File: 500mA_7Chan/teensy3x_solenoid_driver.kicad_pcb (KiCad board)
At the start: 2 copper layers, 88.9 x 50.8 mm, 16 parts, among them J1 Conn_01x02, J2 Conn_01x02, J3 Conn_01x02, J4 Conn_01x02, J5 Conn_01x02, J6 Conn_01x02, J7 Conn_01x02, J8 Conn_02x05_Odd_Even, J9 Jack-DC, M1 VAL**, M2 VAL**, M3 VAL**, M4 VAL**, U1 TEENSY3x, U2 TBD62003A

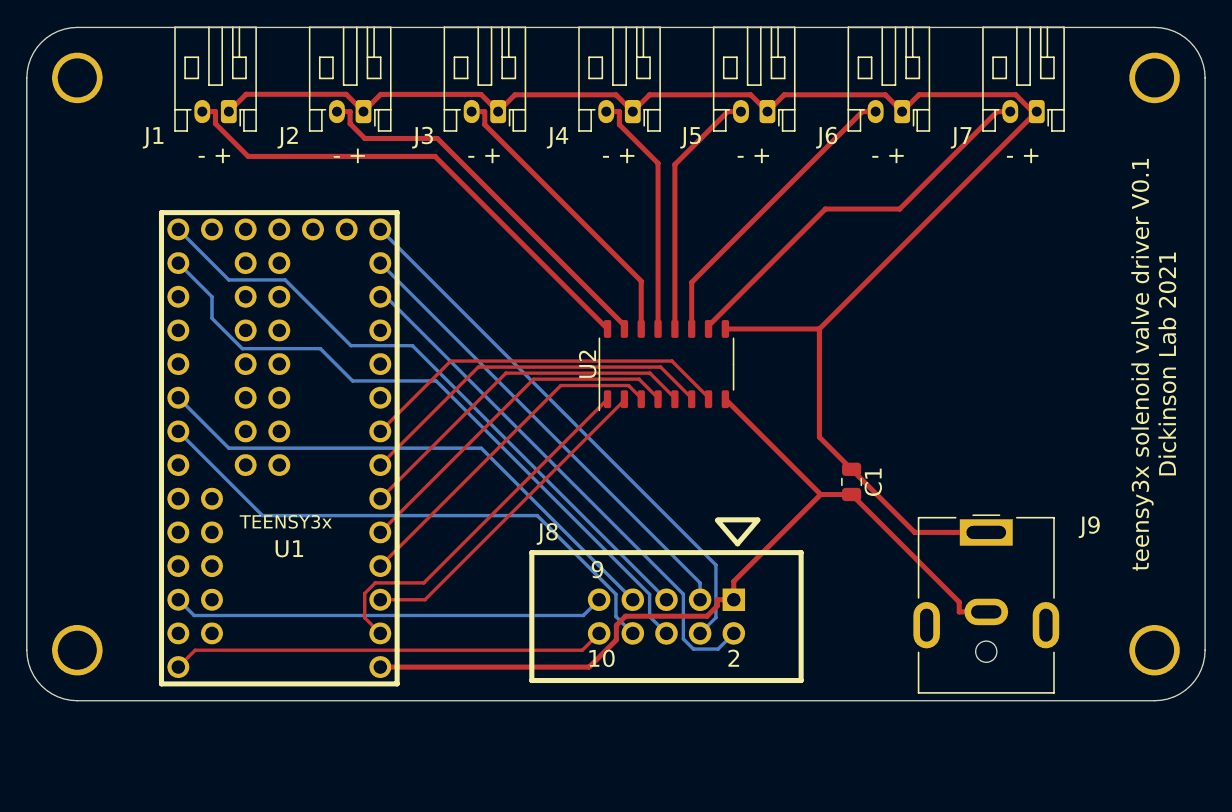
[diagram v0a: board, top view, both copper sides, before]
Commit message: Added finished initial design of 7channel driver.
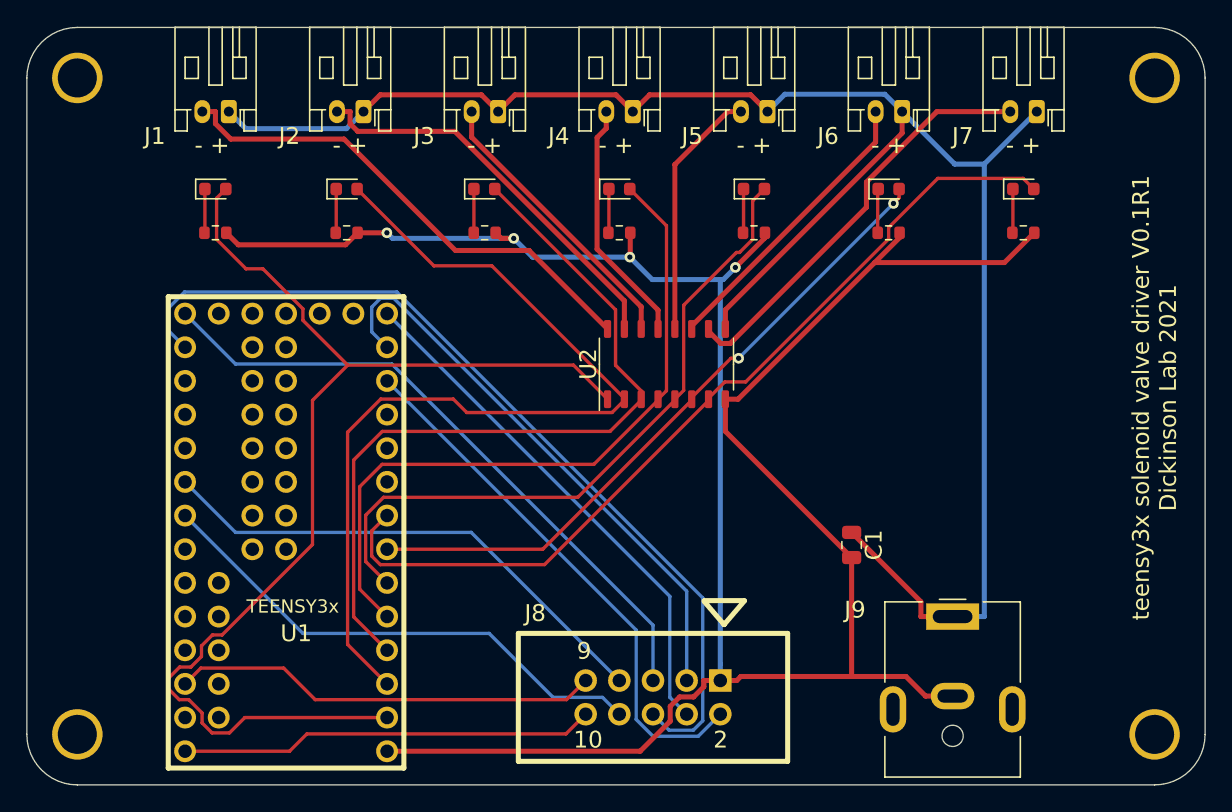
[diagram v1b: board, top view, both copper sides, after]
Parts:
- added D1: LED_ALT, LED_SMD:LED_0603_1608Metric, F.Cu at (65.0, 63.0)
- added D2: LED_ALT, LED_SMD:LED_0603_1608Metric, F.Cu at (74.9, 63.0)
- added D3: LED_ALT, LED_SMD:LED_0603_1608Metric, F.Cu at (85.3, 63.0)
- added D4: LED_ALT, LED_SMD:LED_0603_1608Metric, F.Cu at (95.5, 63.0)
- added D5: LED_ALT, LED_SMD:LED_0603_1608Metric, F.Cu at (105.7, 63.0)
- added D6: LED_ALT, LED_SMD:LED_0603_1608Metric, F.Cu at (115.8, 63.0)
- added D7: LED_ALT, LED_SMD:LED_0603_1608Metric, F.Cu at (126.0, 63.0)
- added R1: 330, Resistor_SMD:R_0603_1608Metric, F.Cu at (65.0, 66.3)
- added R2: 330, Resistor_SMD:R_0603_1608Metric, F.Cu at (74.9, 66.3)
- added R3: 330, Resistor_SMD:R_0603_1608Metric, F.Cu at (85.3, 66.3)
- added R4: 330, Resistor_SMD:R_0603_1608Metric, F.Cu at (95.5, 66.3)
- added R5: 330, Resistor_SMD:R_0603_1608Metric, F.Cu at (105.7, 66.3)
- added R6: 330, Resistor_SMD:R_0603_1608Metric, F.Cu at (115.8, 66.3)
- added R7: 330, Resistor_SMD:R_0603_1608Metric, F.Cu at (126.0, 66.3)
- moved J9 6.84 mm to (120.7, 95.2)
- moved U1 6.37 mm to (70.4, 88.9)
- moved M3 6.35 mm to (135.9, 104.1)
- moved M4 6.35 mm to (54.6, 104.1)
- moved J8 6.18 mm to (98.0, 101.3)
- moved C1 4.76 mm to (113.0, 89.8)
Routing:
- net GND: track 67.1 -> 181.1 mm, vias 0 -> 4
- net Net-(D1-Pad2): track 27.9 -> 88.8 mm
- net Net-(D2-Pad2): track 24.7 -> 69.8 mm
- net Net-(D7-Pad2): track 28.2 -> 66.8 mm
- net Net-(D3-Pad2): track 25.8 -> 59.5 mm
- net Net-(D4-Pad2): track 26.4 -> 53.2 mm
- net Net-(D5-Pad2): track 27.0 -> 51.6 mm
- net Net-(D6-Pad2): track 27.6 -> 50.4 mm, vias 0 -> 2
- net Net-(C1-Pad1): track 121.2 -> 138.9 mm
- net /D14_A0: track 50.3 -> 67.6 mm
- net /D11_MOSI: track 35.4 -> 43.5 mm
- net Net-(D1-Pad1): track 0.00 -> 3.32 mm
- net Net-(D6-Pad1): track 0.00 -> 3.32 mm
- net Net-(D7-Pad1): track 0.00 -> 3.32 mm
- net Net-(D5-Pad1): track 0.00 -> 3.32 mm
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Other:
- board size 88.9 x 50.8 mm -> 88.9 x 57.2 mm
- net class Power: trace_width 0.381 -> 0.635
- board text added: "teensy3x solenoid valve driver V0.1R1 Dickinson Lab 2021"
- board text removed: "teensy3x solenoid valve driver V0.1 Dickinson Lab 2021"
